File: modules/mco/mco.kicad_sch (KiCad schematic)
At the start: 32 parts, among them U1 ATtiny1616-M, U2 MCP6002-xSN, U3 VTL5C

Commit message: Finalized the PCB design of MCO
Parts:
- added R17: 4.7k, Resistor_SMD:R_0402_1005Metric, symbol Device:R
- C1: footprint (none) -> Capacitor_SMD:C_1206_3216Metric
- C2: footprint (none) -> Capacitor_SMD:C_0402_1005Metric
- R1, R10, R11, R12, R13, R14, R15, R16, R2, R3, R4, R5, R6, R7, R8, R9: footprint (none) -> Resistor_SMD:R_0402_1005Metric
- RV1, RV2, RV3: footprint (none) -> BreadModular_Pots:Potentiometer_RV09
- U2: footprint (none) -> Package_SO:SOIC-8-1EP_3.9x4.9mm_P1.27mm_EP2.29x3mm
- U3: footprint OptoDevice:PerkinElmer_VTL5C -> BreadModular_MISC:VTL5C
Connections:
- net UDPI: now also R17.2; no longer U1.19 (~{RESET}/PA0)
- new net: R17.1, U1.19 (~{RESET}/PA0)
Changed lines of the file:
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@@
 	(wire
 		(pts
+			(xy 73.66 46.99) (xy 76.2 46.99)
+		)
+		(stroke
+			(width 0)
+			(type default)
+		)
+	)
+	(wire
+		(pts
 			(xy 245.11 86.36) (xy 248.92 86.36)
 		)
@@
 	(global_label "UDPI"
 		(shape input)
-		(at 66.04 46.99 0)
+		(at 76.2 46.99 0)
 		(fields_autoplaced yes)
 		(effects
@@
 		)
 		(property "Intersheetrefs" "${INTERSHEET_REFS}"
-			(at 73.5005 46.99 0)
+			(at 83.6605 46.99 0)
 			(effects
 				(font
@@
 			)
 		)
-		(property "Footprint" ""
+		(property "Footprint" "Resistor_SMD:R_0402_1005Metric"
 			(at 241.3 88.138 90)
 			(effects
@@
 			)
 		)
-		(property "Footprint" "OptoDevice:PerkinElmer_VTL5C"
+		(property "Footprint" "BreadModular_MISC:VTL5C"
 			(at 62.23 170.18 0)
 			(effects
@@
 			)
 		)
-		(property "Footprint" ""
+		(property "Footprint" "Resistor_SMD:R_0402_1005Metric"
 			(at 142.748 168.91 90)
 			(effects
@@
 			)
 		)
-		(property "Footprint" ""
+		(property "Footprint" "Resistor_SMD:R_0402_1005Metric"
 			(at 139.7 149.098 90)
 			(effects
@@
 			)
 		)
-		(property "Footprint" ""
+		(property "Footprint" "Resistor_SMD:R_0402_1005Metric"
 			(at 72.39 66.548 90)
 			(effects
@@
 		(exclude_from_sim no)
 		(in_bom yes)
-		(on_board yes)
+		(on_board no)
 		(dnp no)
 		(property "Reference" "V2"
@@
 			)
 		)
-		(property "Footprint" ""
+		(property "Footprint" "Capacitor_SMD:C_0402_1005Metric"
 			(at 227.0252 113.03 0)
 			(effects
@@
 			)
 		)
-		(property "Footprint" ""
+		(property "Footprint" "BreadModular_Pots:Potentiometer_RV09"
 			(at 130.81 71.12 0)
 			(effects
@@
 			)
 		)
-		(property "Footprint" ""
+		(property "Footprint" "Package_SO:SOIC-8-1EP_3.9x4.9mm_P1.27mm_EP2.29x3mm"
 			(at 218.44 110.49 0)
 			(effects
@@
 		(exclude_from_sim no)
 		(in_bom yes)
-		(on_board yes)
+		(on_board no)
 		(dnp no)
 		(property "Reference" "V4"
@@
 			)
 		)
-		(property "Footprint" ""
+		(property "Footprint" "Resistor_SMD:R_0402_1005Metric"
 			(at 52.07 182.118 90)
 			(effects
@@
 			)
 		)
-		(property "Footprint" ""
+		(property "Footprint" "Resistor_SMD:R_0402_1005Metric"
 			(at 167.64 135.128 90)
 			(effects
@@
 			)
 		)
-		(property "Footprint" ""
+		(property "Footprint" "Resistor_SMD:R_0402_1005Metric"
 			(at 133.35 179.578 90)
 			(effects
@@
 			)
 		)
-		(property "Footprint" ""
+		(property "Footprint" "BreadModular_Pots:Potentiometer_RV09"
 			(at 50.8 142.24 0)
 			(effects
@@
 			)
 		)
-		(property "Footprint" ""
+		(property "Footprint" "Resistor_SMD:R_0402_1005Metric"
 			(at 76.2 147.828 90)
 			(effects
@@
 			)
 		)
-		(property "Footprint" ""
+		(property "Footprint" "Resistor_SMD:R_0402_1005Metric"
 			(at 72.39 64.008 90)
 			(effects
@@
 			)
 		)
-		(property "Footprint" ""
+		(property "Footprint" "Resistor_SMD:R_0402_1005Metric"
 			(at 55.118 107.95 90)
 			(effects
@@
 			)
 		)
-		(property "Footprint" ""
+		(property "Footprint" "Resistor_SMD:R_0402_1005Metric"
 			(at 55.118 124.46 90)
 			(effects
@@
 			)
 		)
-		(property "Footprint" ""
+		(property "Footprint" "Resistor_SMD:R_0402_1005Metric"
 			(at 86.36 147.828 90)
 			(effects
@@
 			)
 		)
-		(property "Footprint" ""
+		(property "Footprint" "Resistor_SMD:R_0402_1005Metric"
 			(at 152.4 149.098 90)
 			(effects
@@
 			)
 		)
-		(property "Footprint" ""
+		(property "Footprint" "Capacitor_SMD:C_1206_3216Metric"
 			(at 41.91 33.3248 0)
 			(effects
@@
 			)
 		)
-		(property "Footprint" ""
+		(property "Footprint" "Resistor_SMD:R_0402_1005Metric"
 			(at 110.49 189.738 90)
 			(effects
@@
 			)
 		)
-		(property "Footprint" ""
+		(property "Footprint" "Package_SO:SOIC-8-1EP_3.9x4.9mm_P1.27mm_EP2.29x3mm"
 			(at 144.78 133.35 0)
 			(effects
@@
 			)
 		)
-		(property "Footprint" ""
+		(property "Footprint" "Resistor_SMD:R_0402_1005Metric"
 			(at 256.54 88.138 90)
 			(effects
@@
 	)
 	(symbol
+		(lib_id "Device:R")
+		(at 69.85 46.99 90)
+		(unit 1)
+		(exclude_from_sim no)
+		(in_bom yes)
+		(on_board yes)
+		(dnp no)
+		(property "Reference" "R17"
+			(at 69.596 46.99 90)
+			(effects
+				(font
+					(size 1.27 1.27)
+				)
+			)
+		)
+		(property "Value" "4.7k"
+			(at 69.85 45.212 90)
+			(effects
+				(font
+					(size 1.27 1.27)
+				)
+			)
+		)
+		(property "Footprint" "Resistor_SMD:R_0402_1005Metric"
+			(at 69.85 48.768 90)
+			(effects
+				(font
+					(size 1.27 1.27)
+				)
+				(hide yes)
+			)
+		)
+		(property "Datasheet" "~"
+			(at 69.85 46.99 0)
+			(effects
+				(font
+					(size 1.27 1.27)
+				)
+				(hide yes)
+			)
+		)
+		(property "Description" "Resistor"
+			(at 69.85 46.99 0)
+			(effects
+				(font
+					(size 1.27 1.27)
+				)
+				(hide yes)
+			)
+		)
+		(pin "1"
+		)
+		(pin "2"
+		)
+		(instances
+			(project "mco"
+				(path "/b63493d3-5f6d-47e3-845b-87e7090fc1ab"
+					(reference "R17")
+					(unit 1)
+				)
+			)
+		)
+	)
+	(symbol
 		(lib_id "Amplifier_Operational:MCP6002-xSN")
 		(at 107.95 175.26 0)
@@
 			)
 		)
-		(property "Footprint" ""
+		(property "Footprint" "Package_SO:SOIC-8-1EP_3.9x4.9mm_P1.27mm_EP2.29x3mm"
 			(at 107.95 175.26 0)
 			(effects
@@
 			)
 		)
-		(property "Footprint" ""
+		(property "Footprint" "BreadModular_Pots:Potentiometer_RV09"
 			(at 85.09 180.34 0)
 			(effects
@@
 		(exclude_from_sim no)
 		(in_bom yes)
-		(on_board yes)
+		(on_board no)
 		(dnp no)
 		(property "Reference" "V3"
@@
 			)
 		)
-		(property "Footprint" ""
+		(property "Footprint" "Resistor_SMD:R_0402_1005Metric"
 			(at 102.87 116.078 90)
 			(effects

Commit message: Add mco_0.2.0 schematic
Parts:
- removed R10, R14, R16: 1M, Resistor_SMD:R_0402_1005Metric, symbol Device:R
- removed R11, R12: 200k, Resistor_SMD:R_0402_1005Metric, symbol Device:R
- removed R13: 100k, Resistor_SMD:R_0402_1005Metric, symbol Device:R
- removed R15: 510, Resistor_SMD:R_0402_1005Metric, symbol Device:R
- removed R17: 4.7k, Resistor_SMD:R_0402_1005Metric, symbol Device:R
- removed R5: 1k, Resistor_SMD:R_0402_1005Metric, symbol Device:R
- removed R9: 10k, Resistor_SMD:R_0402_1005Metric, symbol Device:R
- removed U1: ATtiny1616-M, Package_DFN_QFN:VQFN-20-1EP_3x3mm_P0.4mm_EP1.7x1.7mm, symbol MCU_Microchip_ATtiny:ATtiny1616-M
- removed U2: MCP6002-xSN, Package_SO:SOIC-8-1EP_3.9x4.9mm_P1.27mm_EP2.29x3mm, symbol Amplifier_Operational:MCP6002-xSN
- removed U3: VTL5C, BreadModular_MISC:VTL5C, symbol Isolator:VTL5C
- removed V3, V4: VPULSE, symbol Simulation_SPICE:VPULSE
- added C3, C4: 0.1uf, symbol Device:C
- added D1: LED, symbol Device:LED
- added R3: 1k, symbol Device:R
- added SW1: MODE SELECT, symbol Switch:SW_SPST
- added U1, U3: MCP6002-xSN, Package_SO:SOIC-8-1EP_3.9x4.9mm_P1.27mm_EP2.29x3mm, symbol Amplifier_Operational:MCP6002-xSN
- added U2: ATtiny1616-M, Package_DFN_QFN:VQFN-20-1EP_3x3mm_P0.4mm_EP1.7x1.7mm, symbol MCU_Microchip_ATtiny:ATtiny1616-M
- C2: value 0.1uf -> 100nf; footprint Capacitor_SMD:C_0402_1005Metric -> Capacitor_SMD:C_1206_3216Metric
- R1: value 1k -> 4.7k; footprint Resistor_SMD:R_0402_1005Metric -> (none)
- R2: footprint Resistor_SMD:R_0402_1005Metric -> (none)
- R4: renamed from R3; footprint Resistor_SMD:R_0402_1005Metric -> (none)
- R5: renamed from R4; footprint Resistor_SMD:R_0402_1005Metric -> (none)
- R6: value 1M -> 330; footprint Resistor_SMD:R_0402_1005Metric -> (none)
- R7, R8: value 1k -> 100k; footprint Resistor_SMD:R_0402_1005Metric -> (none)
- RV1: Comment Detuned -> LOWPASS
- RV2: value 50k -> 1M; Comment Detuned MIX -> CV1_GAIN
- RV3: value 50k -> 1M; Comment CV Curve -> CV2_GAIN
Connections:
- net GND: now also R6.2, RV2.1, RV3.1, C3.2, C4.2, SW1.1 (A), U1.4 (V-), U2.21 (GND), U2.3 (GND), U3.4 (V-); no longer C2.2, RV1.3
- net MIDI: now also U2.11 (PB3)
- net TX: now also U2.10 (PB4)
- net UDPI: now also R1.2
- net V_MID: now also C2.1; no longer RV2.1
- net V_SUPPLY: now also R7.1, R8.1, C3.1, C4.1, U1.8 (V+), U2.4 (VCC), U3.8 (V+); no longer C2.1, RV1.1
- net at R2.1: now also U1.1, U1.2 (-)
- net BUFF_CV1: now reaches RV2.2
- net BUFF_CV1: now also U2.20 (PA1)
- net at R1.1: now also U2.19 (~{RESET}/PA0)
- net BUFF_CV2: now reaches RV3.2
- net BUFF_CV2: now also U2.1 (PA2)
- net CV2: now reaches INPUT1.3 (Pin_3)
- net CV2: now also R8.2, U3.5 (+)
- net at RV3.3: now also U3.6 (-), U3.7
- net DETUNED_OUT renamed CV1
- net CV1: now also INPUT1.2 (Pin_2), U3.3 (+); no longer OUTPUT1.5 (Pin_5)
- net DETUNED_TONE: no longer names the net of RV2.3
- net DETUNED_TONE: now also U3.1, U3.2 (-); no longer R7.1
- net FUNDAMENTAL_TONE: no longer names the net of R6.1
- net FUNDAMENTAL_TONE: now also D1.1 (K)
- net GATE renamed AUDIO_OUT
- net AUDIO_OUT: now also OUTPUT1.1 (Pin_1), OUTPUT1.3 (Pin_3)
- net MIX_CV: no longer names the net of V2.1
- net MIX_CV: no longer INPUT1.2 (Pin_2)
- removed net MIX_OUT: OUTPUT1.1 (Pin_1), R8.2
- net SQUARE_OUT renamed GATE_OUT
- net GATE_OUT: now also OUTPUT1.5 (Pin_5), R3.2
- removed net VELOCITY: OUTPUT1.3 (Pin_3), R1.2
- net V_DETUNED: no longer names the net of RV1.2
- net V_DETUNED: now also C2.2, U1.3 (+)
- new net: U1.5 (+), U2.8 (PA7)
- new net: R3.1, U1.6 (-), U1.7
- new net: RV1.1, U2.7 (PA6)
- new net: SW1.2 (B), U2.17 (PC2)
- new net: D1.2 (A), U2.18 (PC3)
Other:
- note removed: "## Detune Control Controlled how much of detuned of the second waveform. pos = 0.0 -> 12 semitones pos = 1.0 -> 0 semitones"
- note removed: "## Mixing Mixing the fundamental & the detuned waveform together with mix control. Also, we can control the mix via CV."
- moved on the sheet: GND1, INPUT1, OUTPUT1, R4, R5, V1, V_SUPPLY1

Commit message: finalized the PCB design
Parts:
- removed V1: 3.3, symbol Simulation_SPICE:VDC
- removed V2: VSIN, symbol Simulation_SPICE:VSIN
- C2: footprint Capacitor_SMD:C_1206_3216Metric -> Capacitor_SMD:C_0402_1005Metric
- C3, C4: footprint (none) -> Capacitor_SMD:C_0402_1005Metric
- D1: footprint (none) -> LED_SMD:LED_0603_1608Metric
- R1, R2, R3, R4, R5, R6, R7, R8: footprint (none) -> Resistor_SMD:R_0402_1005Metric
- SW1: footprint (none) -> BreadModular_MISC:SPST_TS-1187A-B-A-B
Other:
- moved on the sheet: R7, R8, RV2, RV3, U3A, U3B

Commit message: mco: Rebrand the 0.1.0 version as the new MCO. We removed CV support and it's not needed.
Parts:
- removed C3, C4: 0.1uf, Capacitor_SMD:C_0402_1005Metric, symbol Device:C
- removed D1: LED, LED_SMD:LED_0603_1608Metric, symbol Device:LED
- removed R3: 1k, Resistor_SMD:R_0402_1005Metric, symbol Device:R
- removed RV3: 1M, BreadModular_Pots:Potentiometer_RV09, symbol Device:R_Potentiometer
- removed SW1: MODE SELECT, BreadModular_MISC:SPST_TS-1187A-B-A-B, symbol Switch:SW_SPST
- removed U1: MCP6002-xSN, Package_SO:SOIC-8-1EP_3.9x4.9mm_P1.27mm_EP2.29x3mm, symbol Amplifier_Operational:MCP6002-xSN
- removed U2: ATtiny1616-M, Package_DFN_QFN:VQFN-20-1EP_3x3mm_P0.4mm_EP1.7x1.7mm, symbol MCU_Microchip_ATtiny:ATtiny1616-M
- added R10: 1M, Resistor_SMD:R_0402_1005Metric, symbol Device:R
- added R11, R12: 200k, Resistor_SMD:R_0402_1005Metric, symbol Device:R
- added R17: 4.7k, Resistor_SMD:R_0402_1005Metric, symbol Device:R
- added R5: 1k, Resistor_SMD:R_0402_1005Metric, symbol Device:R
- added U1: ATtiny1616-M, Package_DFN_QFN:VQFN-20-1EP_3x3mm_P0.4mm_EP1.7x1.7mm, symbol MCU_Microchip_ATtiny:ATtiny1616-M
- added V1: 3.3, symbol Simulation_SPICE:VDC
- added V3, V4: VPULSE, symbol Simulation_SPICE:VPULSE
- C2: value 100nf -> 0.1uf
- R1: value 4.7k -> 1k
- R6: value 330 -> 1M
- R7, R8: value 100k -> 1k
- RV1: Comment LOWPASS -> Detuned
- RV2: value 1M -> 50k; Comment CV1_GAIN -> Detuned MIX
- renumbered R4 to R3, R5 to R4
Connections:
- net GND: now also C2.2, RV1.3, U1.21 (GND), U1.3 (GND), V1.2, V3.1, V4.1; no longer R6.2, RV2.1
- net MIDI: now also U1.11 (PB3)
- net TX: now also U1.12 (PB2)
- net UDPI: now also R17.2; no longer R1.2
- net V_MID: now also RV2.1, U3.3 (+); no longer C2.1
- net V_SUPPLY: now also C2.1, RV1.1, U1.4 (VCC), V1.1; no longer R7.1, R8.1
- net at U3.6 (-): no longer U3.7
- net FUNDAMENTAL_TONE: now reaches R6.1
- net FUNDAMENTAL_TONE: now also R5.1, U1.10 (PB4), V3.2
- net V_DETUNED: now reaches RV1.2
- net V_DETUNED: now also U1.14 (PB0); no longer C2.2
- net at R1.1: now also U1.7 (PA6)
- net at R2.1: now also U1.8 (PA7)
- net AUDIO_OUT renamed GATE
- net GATE: no longer OUTPUT1.1 (Pin_1), OUTPUT1.3 (Pin_3)
- net BUFF_CV1: no longer names the net of RV2.2
- net BUFF_CV1: now also R10.1
- removed net CV1: INPUT1.2 (Pin_2), R7.2, U3.3 (+)
- removed net CV2: INPUT1.3 (Pin_3), R8.2, U3.5 (+)
- net GATE_OUT renamed DETUNED_OUT
- net DETUNED_OUT: now also R7.2; no longer OUTPUT1.4 (Pin_4)
- new net: R10.2, R11.1, R6.2, U3.2 (-)
- new net: R11.2, R12.1
- new net: R12.2, R8.1, U3.1
- new net: R17.1, U1.19 (~{RESET}/PA0)
- new net DETUNED_TONE: R7.1, RV2.3, U1.9 (PB5), V4.2
- new net MIX_OUT: OUTPUT1.1 (Pin_1), R8.2
- new net SQUARE_OUT: OUTPUT1.4 (Pin_4), R5.2
- new net VELOCITY: OUTPUT1.3 (Pin_3), R1.2
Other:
- note added: "## Detune Control Controlled how much of detuned of the second waveform. pos = 0.0 -> 12 semitones pos = 1.0 -> 0 semitones"
- note added: "## Mixing Mixing the fundamental & the detuned waveform together with mix control. Also, we can control the mix via CV."
- moved on the sheet: GND1, INPUT1, OUTPUT1, R3, R4, V_SUPPLY1

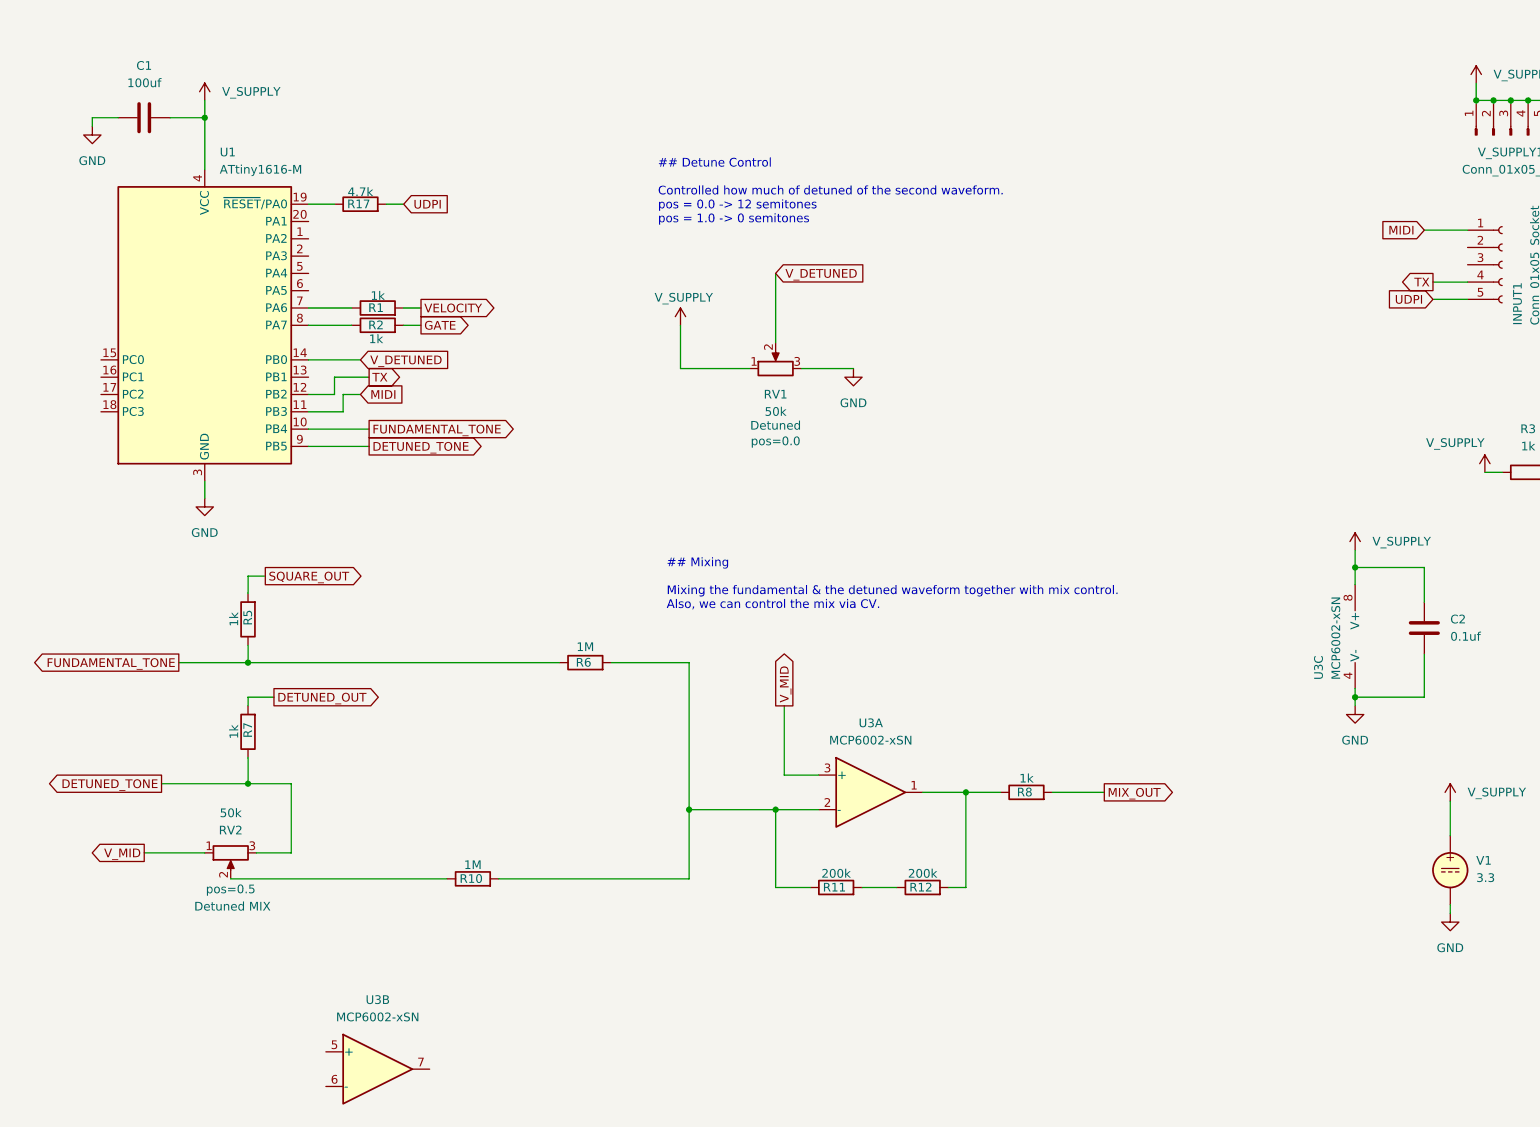
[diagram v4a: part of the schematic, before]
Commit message: Change uc to SOIC
Changing the packaging of the micro to SOIC for easier hand soldering.
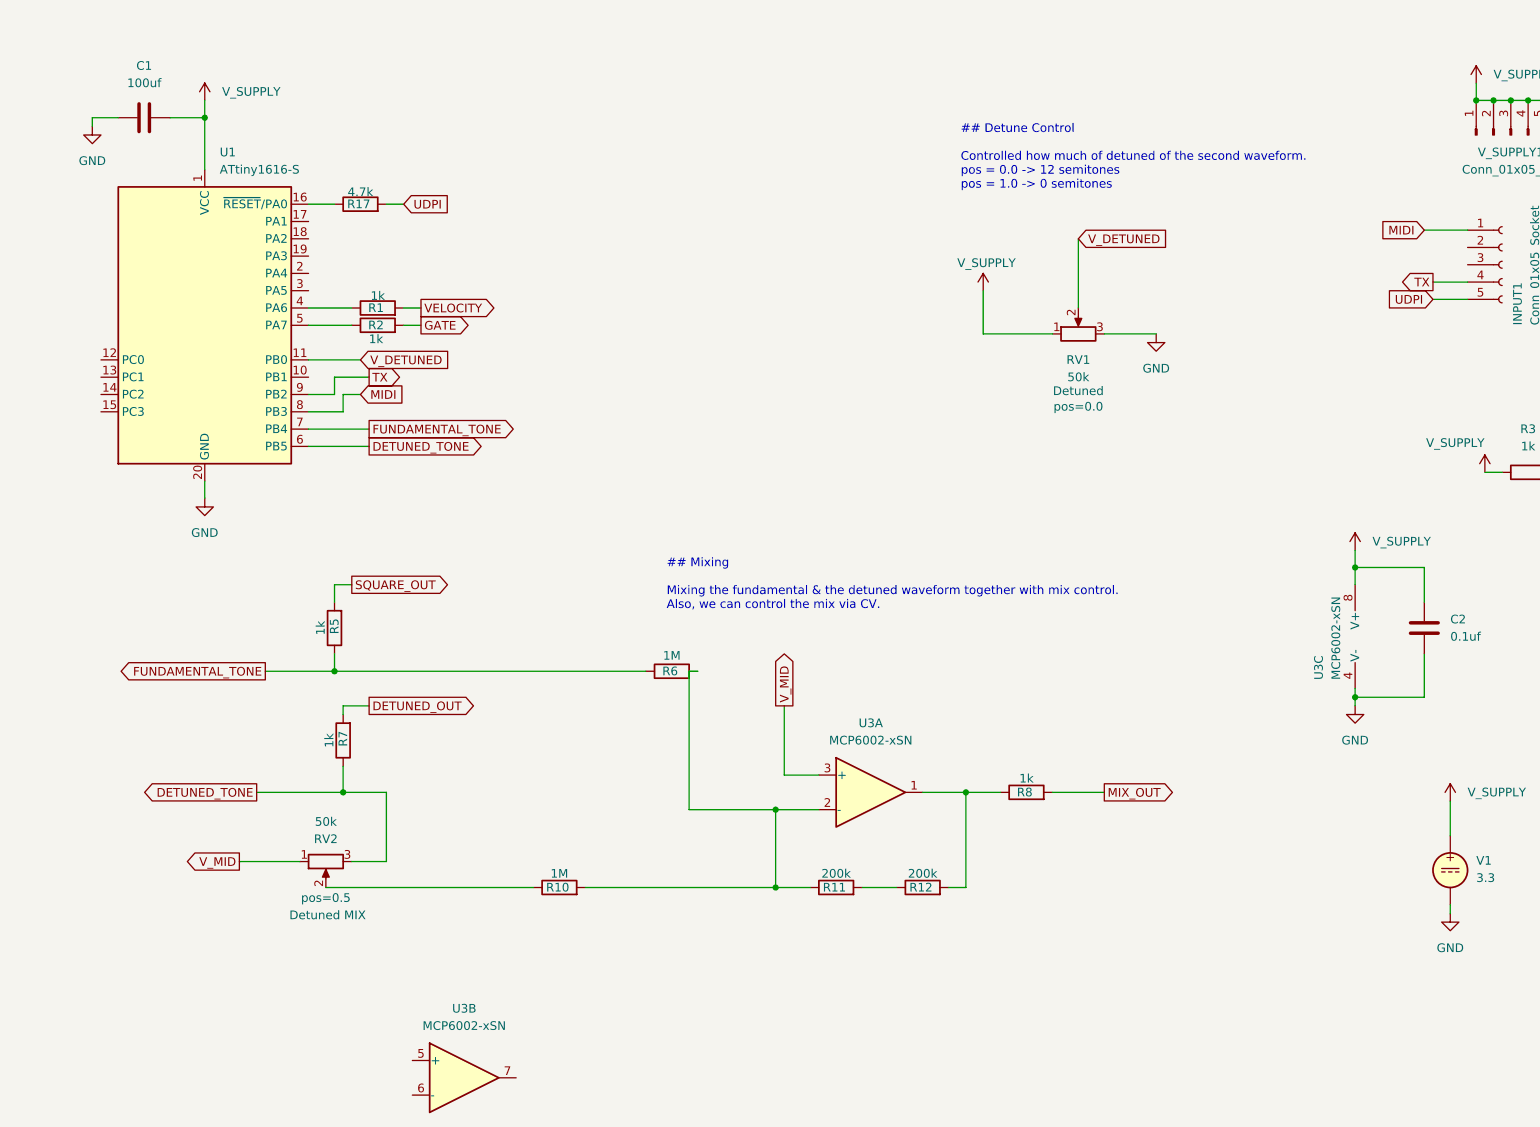
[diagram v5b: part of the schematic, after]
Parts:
- removed U1: ATtiny1616-M, Package_DFN_QFN:VQFN-20-1EP_3x3mm_P0.4mm_EP1.7x1.7mm, symbol MCU_Microchip_ATtiny:ATtiny1616-M
- added U1: ATtiny1616-S, Package_SO:SOIC-20W_7.5x12.8mm_P1.27mm, symbol MCU_Microchip_ATtiny:ATtiny1616-S
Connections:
- net DETUNED_TONE: now also U1.6 (PB5)
- net FUNDAMENTAL_TONE: now also U1.7 (PB4)
- net GND: now also U1.20 (GND)
- net MIDI: now also U1.8 (PB3)
- net TX: now also U1.9 (PB2)
- net V_DETUNED: now also U1.11 (PB0)
- net V_SUPPLY: now also U1.1 (VCC)
- net at R2.1: now also U1.5 (PA7)
- net at R1.1: now also U1.4 (PA6)
- net at R17.1: now also U1.16 (~{RESET}/PA0)
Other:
- moved on the sheet: R10, R5, R6, R7, RV1, RV2, U3B
